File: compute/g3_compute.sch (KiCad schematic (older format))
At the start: 60 parts, among them J101 Pi_Connector, J102 Temp_Connector_1x4, J103 53261-1071, J104 53261-1071, J105 CONSMA001-SMD-G, J107 CONSMA001-SMD-G, J108 Conn_01x07_Male, J109 CONSMA001-SMD-G, Q101 PBSS4140DPN, U101 PA1616D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

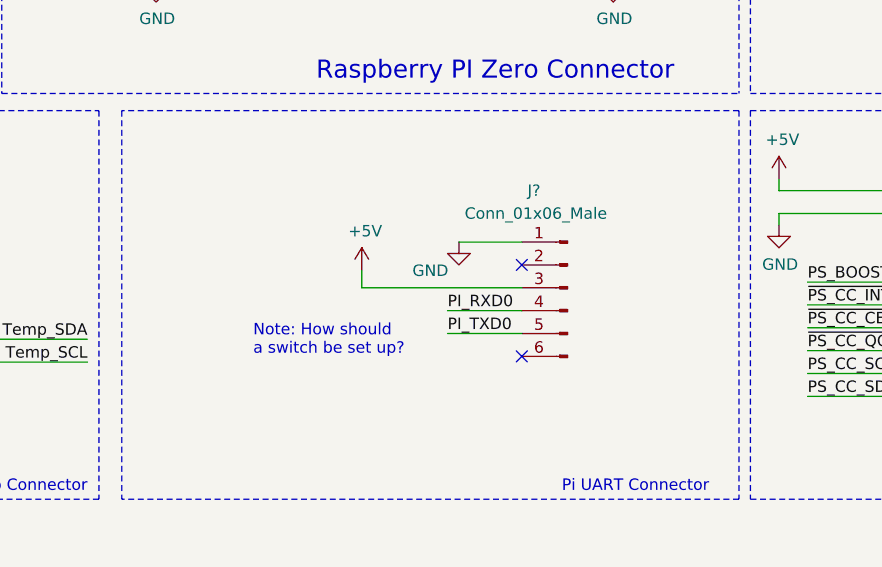
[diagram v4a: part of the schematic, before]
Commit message: Added switch to compute schematic
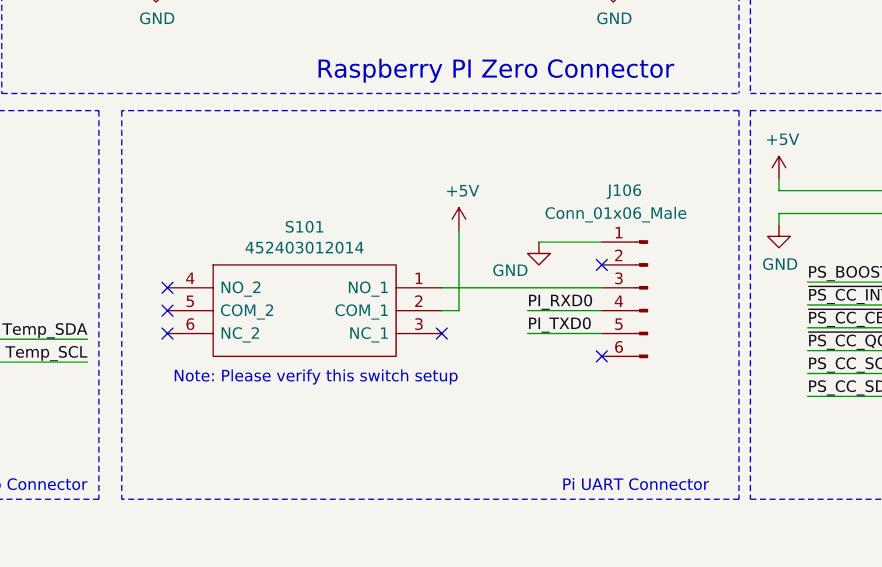
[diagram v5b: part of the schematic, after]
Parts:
- added S101: 452403012014, Perch:452403012014_Switch, symbol 452403012014_Switch:452403012014
- gave numbers to parts that had none: 1
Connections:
- net +5V: now also S101.2 (COM_1); no longer J106.3 (Pin_3)
- new net: J106.3 (Pin_3), S101.1 (NO_1)
- no-connect marks 40 -> 44
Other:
- note added: "Note: Please verify this switch setup\n"
- note removed: "Note: How should\na switch be set up?"
- moved on the sheet: J106
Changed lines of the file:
@@
 L power:GND #PWR0127
 U 1 1 61E6E7A1
-P 6050 5125
-F 0 "#PWR0127" H 6050 4875 50  0001 C CNN
-F 1 "GND" H 5925 5000 50  0000 C CNN
-F 2 "" H 6050 5125 50  0001 C CNN
-F 3 "" H 6050 5125 50  0001 C CNN
-	1    6050 5125
-	1    0    0    -1
-$EndComp
-Wire Wire Line
-	6050 5125 6325 5125
-Wire Wire Line
-	6325 5425 6000 5425
-Wire Wire Line
-	6325 5525 6000 5525
-Text Label 6000 5525 0    50   ~ 0
+P 6400 5125
+F 0 "#PWR0127" H 6400 4875 50  0001 C CNN
+F 1 "GND" H 6275 5000 50  0000 C CNN
+F 2 "" H 6400 5125 50  0001 C CNN
+F 3 "" H 6400 5125 50  0001 C CNN
+	1    6400 5125
+	1    0    0    -1
+$EndComp
+Wire Wire Line
+	6400 5125 6675 5125
+Wire Wire Line
+	6675 5425 6350 5425
+Wire Wire Line
+	6675 5525 6350 5525
+Text Label 6350 5525 0    50   ~ 0
 PI_TXD0
-Text Label 6000 5425 0    50   ~ 0
+Text Label 6350 5425 0    50   ~ 0
 PI_RXD0
 Wire Notes Line
@@
 L power:+5V #PWR0142
 U 1 1 621CBD4E
-P 5625 5250
-F 0 "#PWR0142" H 5625 5100 50  0001 C CNN
-F 1 "+5V" H 5640 5423 50  0000 C CNN
-F 2 "" H 5625 5250 50  0001 C CNN
-F 3 "" H 5625 5250 50  0001 C CNN
-	1    5625 5250
-	1    0    0    -1
-$EndComp
-Wire Wire Line
-	5625 5325 5625 5250
-Wire Wire Line
-	5625 5325 6325 5325
-Text Notes 5150 5625 0    50   ~ 0
-Note: How should\na switch be set up?
+P 6050 5075
+F 0 "#PWR0142" H 6050 4925 50  0001 C CNN
+F 1 "+5V" H 6065 5248 50  0000 C CNN
+F 2 "" H 6050 5075 50  0001 C CNN
+F 3 "" H 6050 5075 50  0001 C CNN
+	1    6050 5075
+	1    0    0    -1
+$EndComp
 Text Notes 1475 900  0    50   ~ 0
 Note: BJT from prev.\nboard. There will be \none unused transistor.
@@
 	2625 3725 2900 3725
 $Comp
-L Connector:Conn_01x06_Male J?
+L Connector:Conn_01x06_Male J106
 U 1 1 62043352
-P 6525 5325
-F 0 "J?" H 6700 5750 50  0000 R CNN
-F 1 "Conn_01x06_Male" H 6975 5650 50  0000 R CNN
-F 2 "Connector_PinHeader_2.54mm:PinHeader_1x06_P2.54mm_Vertical" H 6525 5325 50  0001 C CNN
-F 3 "~" H 6525 5325 50  0001 C CNN
-	1    6525 5325
+P 6875 5325
+F 0 "J106" H 7050 5750 50  0000 R CNN
+F 1 "Conn_01x06_Male" H 7325 5650 50  0000 R CNN
+F 2 "Connector_PinHeader_2.54mm:PinHeader_1x06_P2.54mm_Vertical" H 6875 5325 50  0001 C CNN
+F 3 "~" H 6875 5325 50  0001 C CNN
+	1    6875 5325
 	-1   0    0    -1
 $EndComp
-NoConn ~ 6325 5225
-NoConn ~ 6325 5625
+NoConn ~ 6675 5225
+NoConn ~ 6675 5625
+$Comp
+L 452403012014_Switch:452403012014 S101
+U 1 1 620C2712
+P 4775 5325
+F 0 "S101" H 5375 5590 50  0000 C CNN
+F 1 "452403012014" H 5375 5499 50  0000 C CNN
+F 2 "Perch:452403012014_Switch" H 5825 5425 50  0001 L CNN
+F 3 "https://katalog.we-online.de/em/datasheet/452403012014.pdf" H 5825 5325 50  0001 L CNN
+F 4 "Slide Switches WS-SLSV Slide Switch SMD 7.65mm x 5.5mm" H 5825 5225 50  0001 L CNN "Description"
+	1    4775 5325
+	1    0    0    -1
+$EndComp
+NoConn ~ 5975 5525
+NoConn ~ 4775 5525
+NoConn ~ 4775 5325
+NoConn ~ 4775 5425
+Wire Wire Line
+	6675 5325 5975 5325
+Wire Wire Line
+	5975 5425 6050 5425
+Wire Wire Line
+	6050 5425 6050 5075
+Text Notes 4800 5750 0    50   ~ 0
+Note: Please verify this switch setup\n
 $EndSCHEMATC

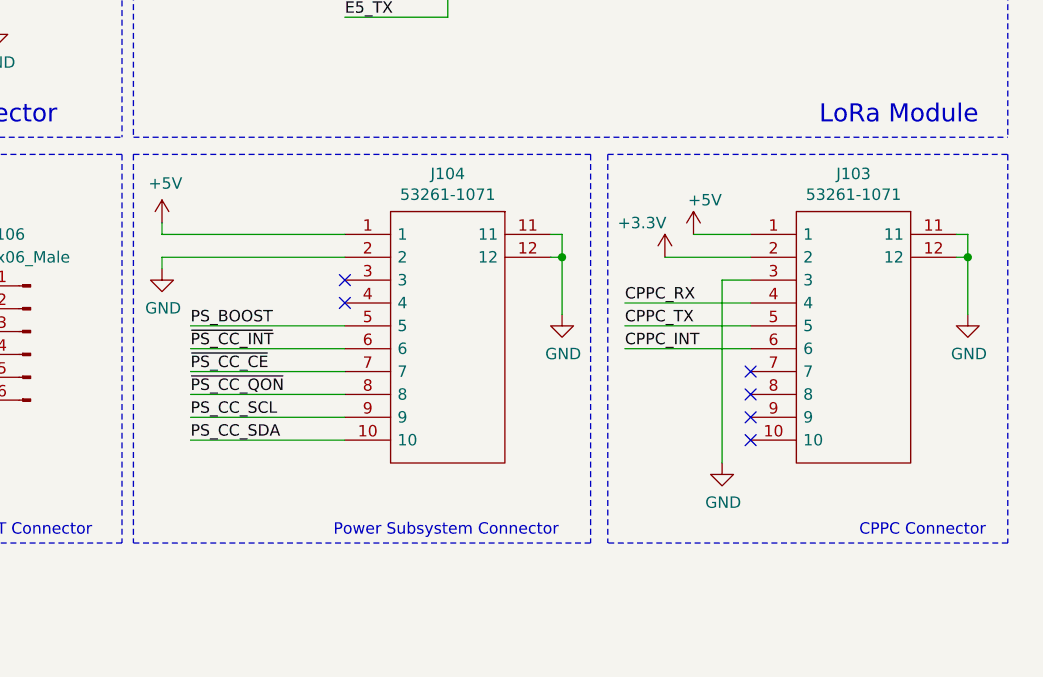
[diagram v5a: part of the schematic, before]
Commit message: Changed out the two molex connectors to what is wanted in the feedback
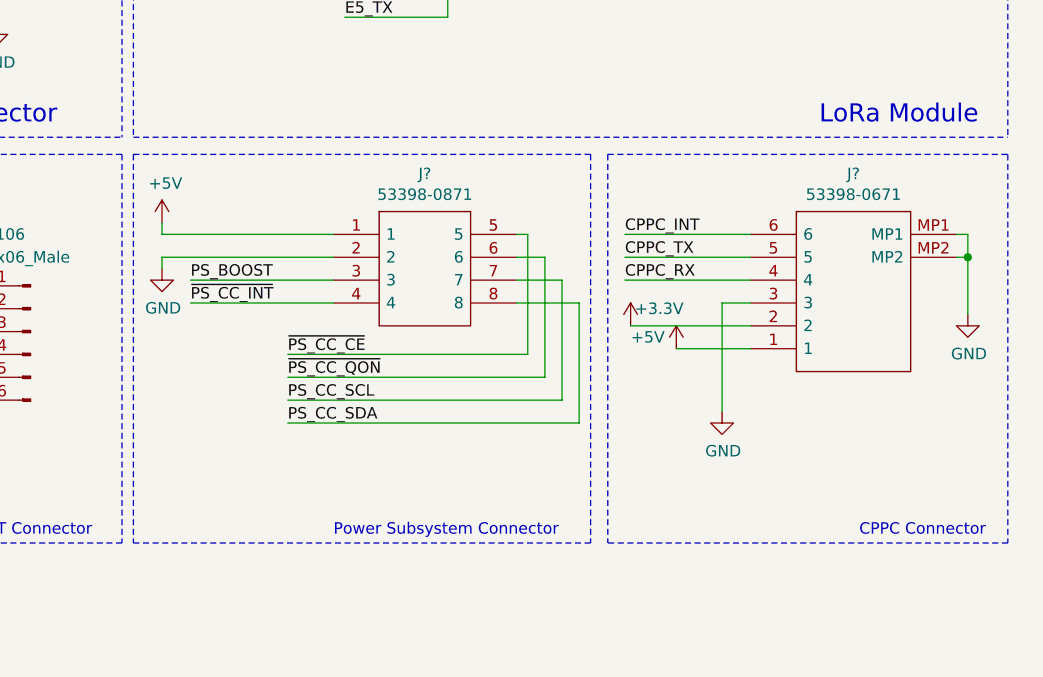
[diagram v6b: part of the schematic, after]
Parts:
- removed J103, J104: 53261-1071, Perch:532611071_Molex, symbol 53261-1071:53261-1071
- added J?: 53398-0871, Perch:53398-0871_Molex, symbol 533980871_Molex:53398-0871
- added J?: 53398-0671, Perch:533980671_Molex, symbol 533980671_Molex:53398-0671
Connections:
- net +3V3: now also J?.2
- net +5V: now also J?.1, J?.1
- net CPPC_INT: now also J?.6
- net CPPC_RX: now also J?.4
- net CPPC_TX: now also J?.5
- net GND: now also J?.2, J?.3, J?.MP1, J?.MP2
- net PS_BOOST: now also J?.3
- net PS_CC_SCL: now also J?.7
- net PS_CC_SDA: now also J?.8
- net ~PS_CC_CE: now also J?.5
- net ~PS_CC_INT: now also J?.4
- net ~PS_CC_QON: now also J?.6
- no-connect marks 44 -> 38
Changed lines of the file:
@@
 Wire Wire Line
 	2050 4050 2500 4050
-Text Label 9475 5200 0    50   ~ 0
+Text Label 9475 5100 0    50   ~ 0
 CPPC_RX
-Text Label 9475 5300 0    50   ~ 0
+Text Label 9475 5000 0    50   ~ 0
 CPPC_TX
-Text Label 9475 5400 0    50   ~ 0
+Text Label 9475 4900 0    50   ~ 0
 CPPC_INT
 Text Notes 5425 4425 0    79   ~ 0
@@
 L power:+5V #PWR0129
 U 1 1 61DF7584
-P 9775 4900
-F 0 "#PWR0129" H 9775 4750 50  0001 C CNN
-F 1 "+5V" H 9825 5050 50  0000 C CNN
-F 2 "" H 9775 4900 50  0001 C CNN
-F 3 "" H 9775 4900 50  0001 C CNN
-	1    9775 4900
-	1    0    0    -1
+P 9700 5400
+F 0 "#PWR0129" H 9700 5250 50  0001 C CNN
+F 1 "+5V" H 9825 5450 50  0000 C CNN
+F 2 "" H 9700 5400 50  0001 C CNN
+F 3 "" H 9700 5400 50  0001 C CNN
+	1    9700 5400
+	-1   0    0    -1
 $EndComp
 $Comp
 L power:+3.3V #PWR0130
 U 1 1 61DF7A7B
-P 9650 5000
-F 0 "#PWR0130" H 9650 4850 50  0001 C CNN
-F 1 "+3.3V" H 9550 5150 50  0000 C CNN
-F 2 "" H 9650 5000 50  0001 C CNN
-F 3 "" H 9650 5000 50  0001 C CNN
-	1    9650 5000
-	1    0    0    -1
+P 9500 5300
+F 0 "#PWR0130" H 9500 5150 50  0001 C CNN
+F 1 "+3.3V" H 9375 5375 50  0000 C CNN
+F 2 "" H 9500 5300 50  0001 C CNN
+F 3 "" H 9500 5300 50  0001 C CNN
+	1    9500 5300
+	-1   0    0    -1
 $EndComp
 $Comp
 L power:GND #PWR0115
 U 1 1 61EE3A32
-P 9900 5900
-F 0 "#PWR0115" H 9900 5650 50  0001 C CNN
-F 1 "GND" H 9905 5727 50  0000 C CNN
-F 2 "" H 9900 5900 50  0001 C CNN
-F 3 "" H 9900 5900 50  0001 C CNN
-	1    9900 5900
-	1    0    0    -1
-$EndComp
-Wire Wire Line
-	9900 5100 9900 5900
+P 9900 5675
+F 0 "#PWR0115" H 9900 5425 50  0001 C CNN
+F 1 "GND" H 9905 5502 50  0000 C CNN
+F 2 "" H 9900 5675 50  0001 C CNN
+F 3 "" H 9900 5675 50  0001 C CNN
+	1    9900 5675
+	1    0    0    -1
+$EndComp
 Wire Wire Line
 	2500 3725 2625 3725
 Wire Wire Line
 	2900 3625 2900 3725
-$Comp
-L 53261-1071:53261-1071 J103
-U 1 1 61E456C4
-P 10925 4900
-F 0 "J103" H 11375 5165 50  0000 C CNN
-F 1 "53261-1071" H 11375 5074 50  0000 C CNN
-F 2 "Perch:532611071_Molex" H 11675 5000 50  0001 L CNN
-F 3 "https://www.molex.com/webdocs/datasheets/pdf/en-us/0532611071_PCB_HEADERS.pdf" H 11675 4900 50  0001 L CNN
-F 4 "10 way SMT r/a header Molex PICOBLADE Series, Series Number 53261, 1.25mm Pitch 10 Way 1 Row Shrouded Right Angle PCB Header, Surface Mount" H 11675 4800 50  0001 L CNN "Description"
-F 5 "Molex" H 10925 4900 50  0001 C CNN "MFN"
-F 6 "53261-1071" H 10925 4900 50  0001 C CNN "MFP"
-F 7 "https://www.mouser.com/ProductDetail/Molex/53261-1071?qs=%252B72YyncTwW%252Bzs3RwZTiukQ%3D%3D" H 10925 4900 50  0001 C CNN "S1PL"
-F 8 "538-53261-1071" H 10925 4900 50  0001 C CNN "S1PN"
-F 9 "https://www.heilind.com/search/result?q=53261-1071&manufacturer=5031&utm_source=molex.com&utm_medium=referral&utm_campaign=molex-disty-stock-check" H 10925 4900 50  0001 C CNN "S2PL"
-F 10 "MOL53261-1071.P" H 10925 4900 50  0001 C CNN "S2PN"
-	1    10925 4900
-	-1   0    0    -1
-$EndComp
 Text Notes 9625 3850 0    50   ~ 0
 Note: \nProbably used as filters, do \nnot load until needed
@@
 	1    0    0    -1
 $EndComp
-Text Label 7575 5600 0    50   ~ 0
+Text Label 8000 5525 0    50   ~ 0
 ~PS_CC_QON
-Text Label 7575 5700 0    50   ~ 0
+Text Label 8000 5625 0    50   ~ 0
 PS_CC_SCL
-Text Label 7575 5800 0    50   ~ 0
+Text Label 8000 5725 0    50   ~ 0
 PS_CC_SDA
-Text Label 7575 5400 0    50   ~ 0
+Text Label 7575 5200 0    50   ~ 0
 ~PS_CC_INT
-Text Label 7575 5500 0    50   ~ 0
+Text Label 8000 5425 0    50   ~ 0
 ~PS_CC_CE
 Wire Wire Line
-	9775 4900 10025 4900
-Wire Wire Line
-	9650 5000 10025 5000
-Wire Wire Line
-	9900 5100 10025 5100
-Wire Wire Line
-	9475 5200 10025 5200
-Wire Wire Line
-	9475 5300 10025 5300
-Wire Wire Line
-	9475 5400 10025 5400
-$Comp
-L 53261-1071:53261-1071 J104
-U 1 1 61E5BCC4
-P 9150 4900
-F 0 "J104" H 9600 5165 50  0000 C CNN
-F 1 "53261-1071" H 9600 5074 50  0000 C CNN
-F 2 "Perch:532611071_Molex" H 9900 5000 50  0001 L CNN
-F 3 "https://www.molex.com/webdocs/datasheets/pdf/en-us/0532611071_PCB_HEADERS.pdf" H 9900 4900 50  0001 L CNN
-F 4 "10 way SMT r/a header Molex PICOBLADE Series, Series Number 53261, 1.25mm Pitch 10 Way 1 Row Shrouded Right Angle PCB Header, Surface Mount" H 9900 4800 50  0001 L CNN "Description"
-F 5 "Molex" H 9150 4900 50  0001 C CNN "MFN"
-F 6 "53261-1071" H 9150 4900 50  0001 C CNN "MFP"
-F 7 "https://www.mouser.com/ProductDetail/Molex/53261-1071?qs=%252B72YyncTwW%252Bzs3RwZTiukQ%3D%3D" H 9150 4900 50  0001 C CNN "S1PL"
-F 8 "538-53261-1071" H 9150 4900 50  0001 C CNN "S1PN"
-F 9 "https://www.heilind.com/search/result?q=53261-1071&manufacturer=5031&utm_source=molex.com&utm_medium=referral&utm_campaign=molex-disty-stock-check" H 9150 4900 50  0001 C CNN "S2PL"
-F 10 "MOL53261-1071.P" H 9150 4900 50  0001 C CNN "S2PN"
-	1    9150 4900
-	-1   0    0    -1
-$EndComp
-Wire Wire Line
-	7450 4900 8250 4900
-Wire Wire Line
-	7450 5000 8250 5000
-Wire Wire Line
-	7575 5400 8250 5400
-Wire Wire Line
-	7575 5500 8250 5500
-Wire Wire Line
-	7575 5600 8250 5600
-Wire Wire Line
-	7575 5700 8250 5700
-Wire Wire Line
-	7575 5800 8250 5800
+	9700 5400 10025 5400
+Wire Wire Line
+	9500 5300 10025 5300
+Wire Wire Line
+	9900 5200 10025 5200
+Wire Wire Line
+	9475 5100 10025 5100
+Wire Wire Line
+	9475 5000 10025 5000
+Wire Wire Line
+	9475 4900 10025 4900
+Wire Wire Line
+	7450 4900 8200 4900
+Wire Wire Line
+	7450 5000 8200 5000
+Wire Wire Line
+	7575 5200 8200 5200
 $Comp
 L power:GND #PWR0132
@@
 	1    0    0    -1
 $EndComp
-$Comp
-L power:GND #PWR0131
-U 1 1 61EDF3A5
-P 9200 5250
-F 0 "#PWR0131" H 9200 5000 50  0001 C CNN
-F 1 "GND" H 9205 5077 50  0000 C CNN
-F 2 "" H 9200 5250 50  0001 C CNN
-F 3 "" H 9200 5250 50  0001 C CNN
-	1    9200 5250
-	1    0    0    -1
-$EndComp
-Wire Wire Line
-	9200 5250 9200 5000
-Wire Wire Line
-	9200 4900 9150 4900
-Wire Wire Line
-	9150 5000 9200 5000
-Connection ~ 9200 5000
-Wire Wire Line
-	9200 5000 9200 4900
 Wire Wire Line
 	10975 5250 10975 5000
@@
 Text Label 1200 6325 2    50   ~ 0
 CPPC_TX
-NoConn ~ 10025 5500
-NoConn ~ 10025 5600
-NoConn ~ 10025 5700
-NoConn ~ 10025 5800
 Wire Wire Line
 	8600 3850 8250 3850
@@
 Wire Wire Line
 	7450 5000 7450 5050
-NoConn ~ 8250 5200
-NoConn ~ 8250 5100
 Text Label 7125 2175 2    50   ~ 0
 PI_TXD0
@@
 	7025 1175 7025 1250
 Wire Wire Line
-	8250 5300 7575 5300
-Text Label 7575 5300 0    50   ~ 0
+	8200 5100 7575 5100
+Text Label 7575 5100 0    50   ~ 0
 PS_BOOST
 NoConn ~ 3625 1600
@@
 Text Notes 4800 5750 0    50   ~ 0
 Note: Please verify this switch setup\n
+$Comp
+L 533980871_Molex:53398-0871 J?
+U 1 1 6227437C
+P 8200 4900
+F 0 "J?" H 8600 5165 50  0000 C CNN
+F 1 "53398-0871" H 8600 5074 50  0000 C CNN
+F 2 "Perch:53398-0871_Molex" H 8850 5000 50  0001 L CNN
+F 3 "http://www.molex.com/webdocs/datasheets/pdf/en-us/0533980871_PCB_HEADERS.pdf" H 8850 4900 50  0001 L CNN
+	1    8200 4900
+	1    0    0    -1
+$EndComp
+Wire Wire Line
+	9000 4900 9050 4900
+Wire Wire Line
+	9050 4900 9050 5425
+Wire Wire Line
+	8000 5425 9050 5425
+Wire Wire Line
+	9125 5525 9125 5000
+Wire Wire Line
+	9125 5000 9000 5000
+Wire Wire Line
+	8000 5525 9125 5525
+Wire Wire Line
+	9000 5100 9200 5100
+Wire Wire Line
+	9200 5100 9200 5625
+Wire Wire Line
+	8000 5625 9200 5625
+Wire Wire Line
+	9275 5725 9275 5200
+Wire Wire Line
+	9275 5200 9000 5200
+Wire Wire Line
+	8000 5725 9275 5725
+$Comp
+L 533980671_Molex:53398-0671 J?
+U 1 1 6232A005
+P 10025 4900
+F 0 "J?" H 10475 5165 50  0000 C CNN
+F 1 "53398-0671" H 10475 5074 50  0000 C CNN
+F 2 "Perch:533980671_Molex" H 10775 5000 50  0001 L CNN
+F 3 "https://www.mouser.co.uk/datasheet/2/276/0533980671_PCB_HEADERS-256970.pdf" H 10775 4900 50  0001 L CNN
+F 4 "Headers & Wire Housings VERTICAL HDR SMT 6P" H 10775 4800 50  0001 L CNN "Description"
+	1    10025 4900
+	1    0    0    -1
+$EndComp
+Wire Wire Line
+	9900 5200 9900 5675
 $EndSCHEMATC

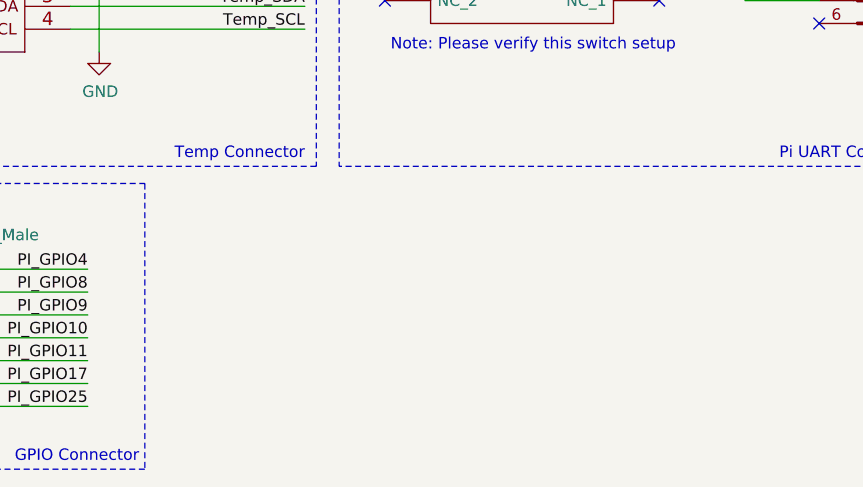
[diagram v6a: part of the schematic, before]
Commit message: Added mounting holes
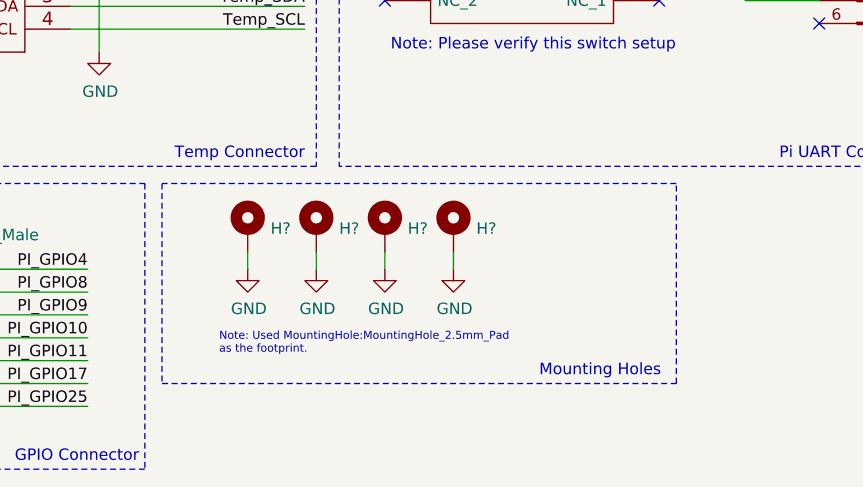
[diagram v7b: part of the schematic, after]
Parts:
- added H? (x4): MountingHole_Pad, MountingHole:MountingHole_2.5mm_Pad, symbol Mechanical:MountingHole_Pad
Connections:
- net GND: now also H?.1, H?.1, H?.1, H?.1
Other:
- note added: "Mounting Holes"
- note added: "Note: Used MountingHole:MountingHole_2.5mm_Pad\nas the footprint."
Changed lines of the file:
@@
 Wire Wire Line
 	9900 5200 9900 5675
+$Comp
+L Mechanical:MountingHole_Pad H?
+U 1 1 6242761B
+P 4175 6525
+F 0 "H?" H 4275 6528 50  0000 L CNN
+F 1 "MountingHole_Pad" H 4275 6483 50  0001 L CNN
+F 2 "MountingHole:MountingHole_2.5mm_Pad" H 4175 6525 50  0001 C CNN
+F 3 "~" H 4175 6525 50  0001 C CNN
+	1    4175 6525
+	1    0    0    -1
+$EndComp
+$Comp
+L Mechanical:MountingHole_Pad H?
+U 1 1 624282C9
+P 4475 6525
+F 0 "H?" H 4575 6528 50  0000 L CNN
+F 1 "MountingHole_Pad" H 4575 6483 50  0001 L CNN
+F 2 "MountingHole:MountingHole_2.5mm_Pad" H 4475 6525 50  0001 C CNN
+F 3 "~" H 4475 6525 50  0001 C CNN
+	1    4475 6525
+	1    0    0    -1
+$EndComp
+$Comp
+L Mechanical:MountingHole_Pad H?
+U 1 1 6242854A
+P 4775 6525
+F 0 "H?" H 4875 6528 50  0000 L CNN
+F 1 "MountingHole_Pad" H 4875 6483 50  0001 L CNN
+F 2 "MountingHole:MountingHole_2.5mm_Pad" H 4775 6525 50  0001 C CNN
+F 3 "~" H 4775 6525 50  0001 C CNN
+	1    4775 6525
+	1    0    0    -1
+$EndComp
+$Comp
+L Mechanical:MountingHole_Pad H?
+U 1 1 624288B4
+P 5075 6525
+F 0 "H?" H 5175 6528 50  0000 L CNN
+F 1 "MountingHole_Pad" H 5175 6483 50  0001 L CNN
+F 2 "MountingHole:MountingHole_2.5mm_Pad" H 5075 6525 50  0001 C CNN
+F 3 "~" H 5075 6525 50  0001 C CNN
+	1    5075 6525
+	1    0    0    -1
+$EndComp
+Wire Wire Line
+	4175 6625 4175 6700
+$Comp
+L power:GND #PWR?
+U 1 1 6243AD3B
+P 4175 6700
+F 0 "#PWR?" H 4175 6450 50  0001 C CNN
+F 1 "GND" H 4180 6527 50  0000 C CNN
+F 2 "" H 4175 6700 50  0001 C CNN
+F 3 "" H 4175 6700 50  0001 C CNN
+	1    4175 6700
+	1    0    0    -1
+$EndComp
+Wire Wire Line
+	4475 6625 4475 6700
+$Comp
+L power:GND #PWR?
+U 1 1 6243B990
+P 4475 6700
+F 0 "#PWR?" H 4475 6450 50  0001 C CNN
+F 1 "GND" H 4480 6527 50  0000 C CNN
+F 2 "" H 4475 6700 50  0001 C CNN
+F 3 "" H 4475 6700 50  0001 C CNN
+	1    4475 6700
+	1    0    0    -1
+$EndComp
+Wire Wire Line
+	4775 6625 4775 6700
+$Comp
+L power:GND #PWR?
+U 1 1 6244D81C
+P 4775 6700
+F 0 "#PWR?" H 4775 6450 50  0001 C CNN
+F 1 "GND" H 4780 6527 50  0000 C CNN
+F 2 "" H 4775 6700 50  0001 C CNN
+F 3 "" H 4775 6700 50  0001 C CNN
+	1    4775 6700
+	1    0    0    -1
+$EndComp
+Wire Wire Line
+	5075 6625 5075 6700
+$Comp
+L power:GND #PWR?
+U 1 1 6245F779
+P 5075 6700
+F 0 "#PWR?" H 5075 6450 50  0001 C CNN
+F 1 "GND" H 5080 6527 50  0000 C CNN
+F 2 "" H 5075 6700 50  0001 C CNN
+F 3 "" H 5075 6700 50  0001 C CNN
+	1    5075 6700
+	1    0    0    -1
+$EndComp
+Text Notes 4050 7075 0    35   ~ 0
+Note: Used MountingHole:MountingHole_2.5mm_Pad\nas the footprint.
+Text Notes 5450 7175 0    50   ~ 0
+Mounting Holes
+Wire Notes Line
+	3800 7200 6050 7200
+Wire Notes Line
+	6050 7200 6050 6325
+Wire Notes Line
+	6050 6325 3800 6325
+Wire Notes Line
+	3800 6325 3800 7200
 $EndSCHEMATC
